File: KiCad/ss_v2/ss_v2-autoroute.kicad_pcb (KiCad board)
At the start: 2 copper layers, 59 parts, among them J1 PJ-313D-B-SMT, J2 UJC-HP-M-G-5-MSMT-TR, J3 DC-005-20A, J4 Conn_02x03_Top_Bottom, J5 Conn_02x03_Counter_Clockwise, J6 Conn_01x08_Pin, J7 Conn_01x04, Q1 BSN20, Q2 IRF7416TRPBF, Q3 BSN20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

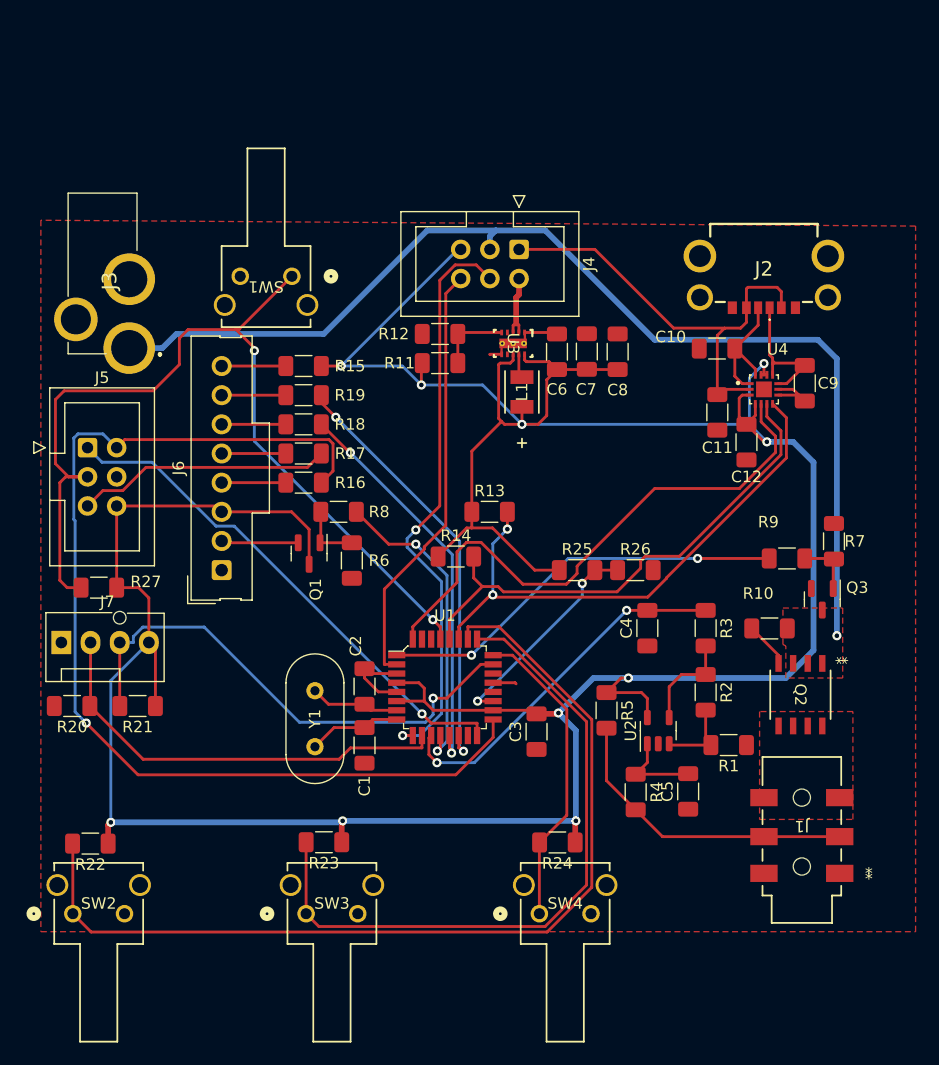
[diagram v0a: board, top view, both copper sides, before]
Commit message: Autorouting verbessert
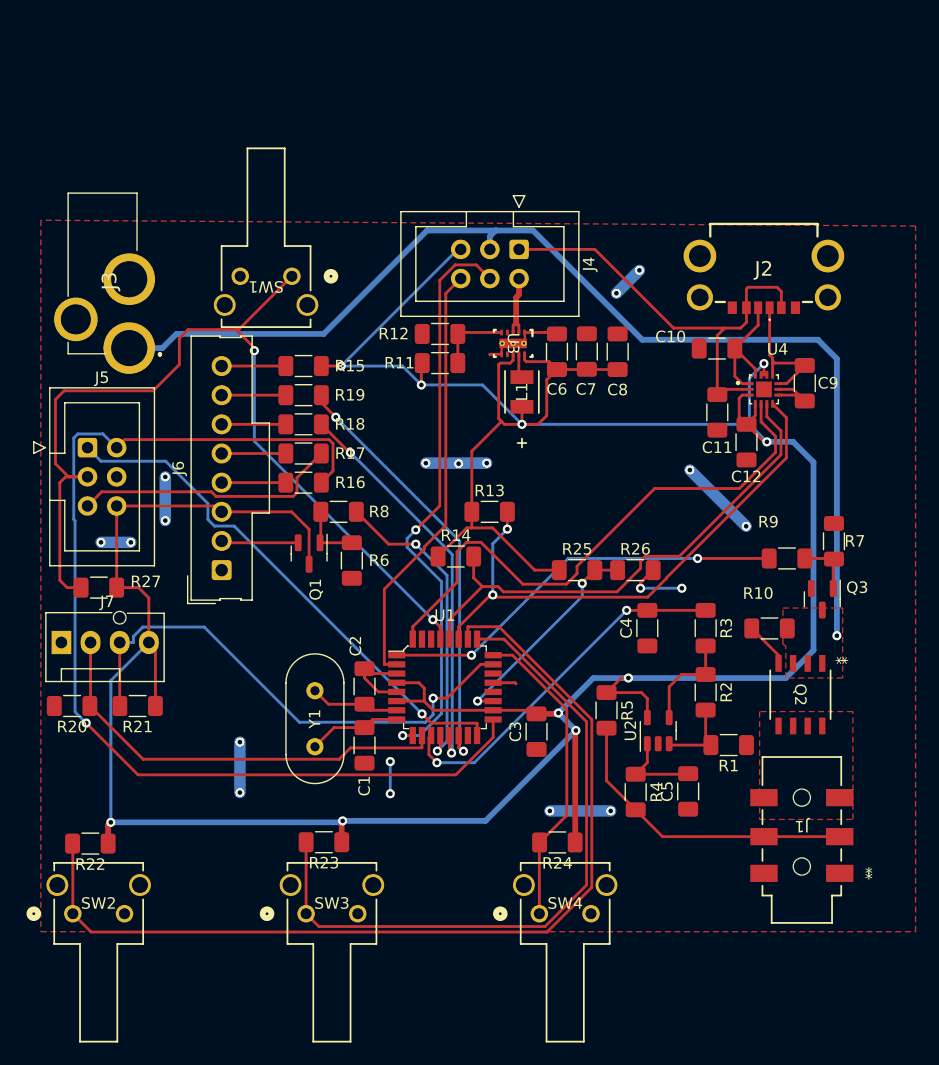
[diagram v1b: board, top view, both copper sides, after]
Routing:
- net GND: track 18.3 -> 57.9 mm, vias 0 -> 19
- net +5V: track 310.1 -> 313.3 mm
- net mosi: track 22.3 -> 23.3 mm
- net miso: track 45.0 -> 45.8 mm

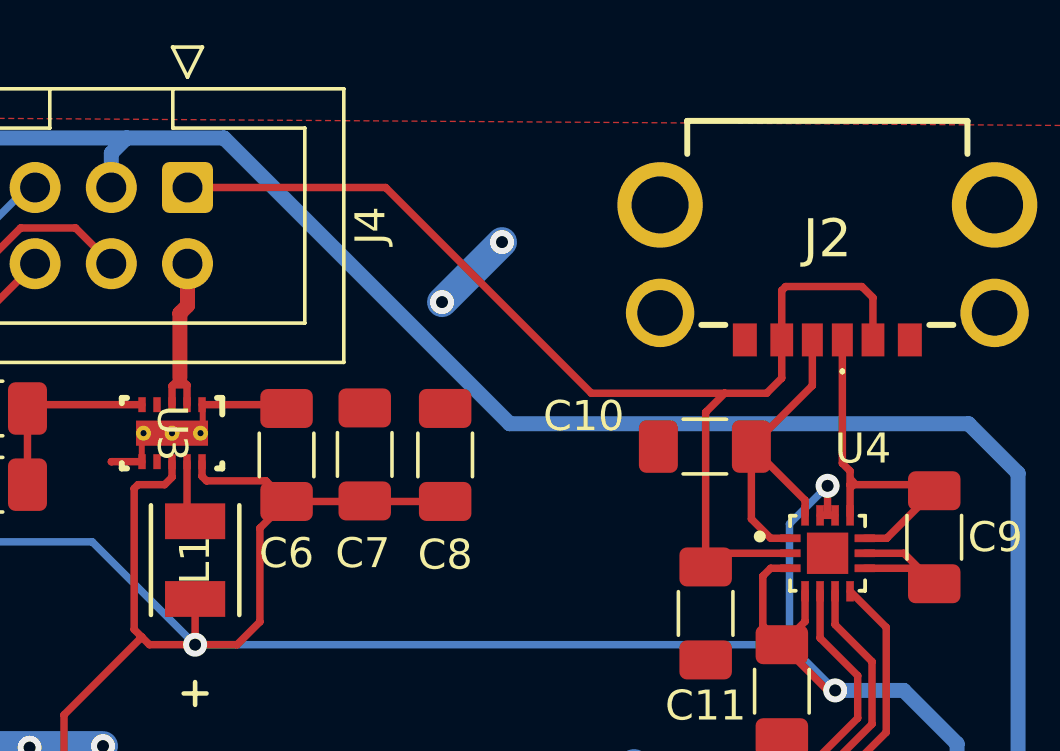
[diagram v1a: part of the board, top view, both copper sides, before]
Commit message: Autorouting verbessert
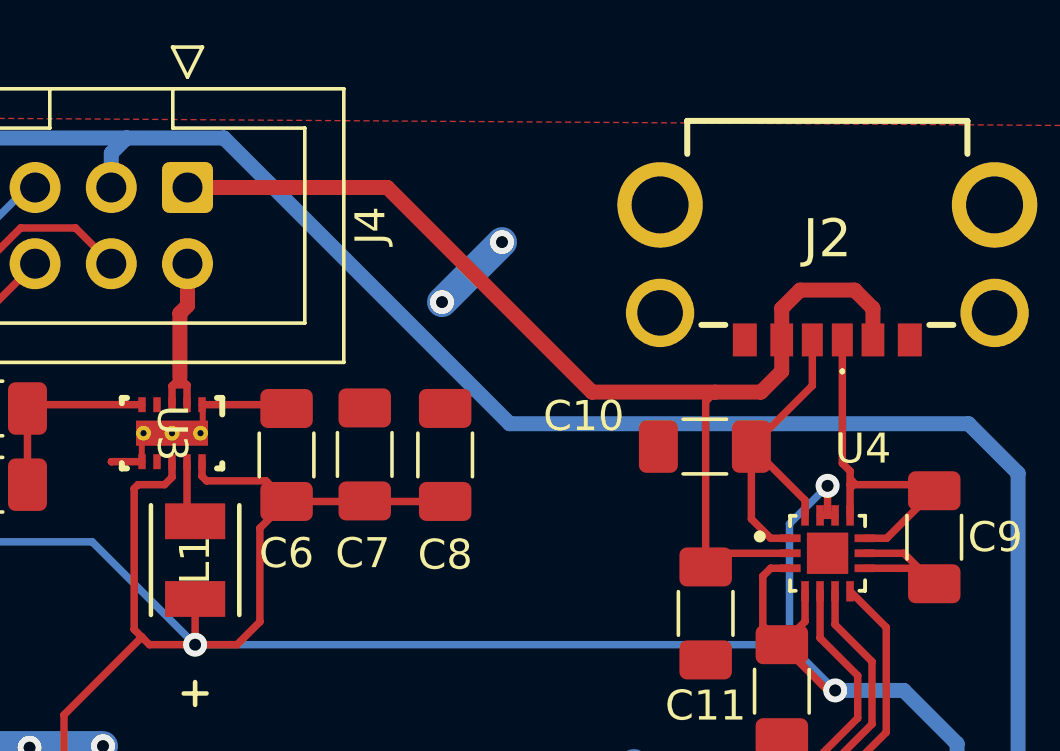
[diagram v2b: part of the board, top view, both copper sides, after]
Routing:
- net VBUS: track 39.5 -> 38.6 mm
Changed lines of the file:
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@@
   (segment (start 249.055 80.272) (end 248.412 79.629) (width 0.25) (layer "F.Cu") (net 8))
   (segment (start 250.202 79.006) (end 248.412 77.216) (width 0.25) (layer "F.Cu") (net 8))
-  (segment (start 243.078 75.438) (end 247.523 75.438) (width 0.25) (layer "F.Cu") (net 9))
-  (segment (start 246.888 81.228) (end 246.888 76.073) (width 0.25) (layer "F.Cu") (net 9))
+  (segment (start 251.854 72) (end 252.464 72.61) (width 0.5) (layer "F.Cu") (net 9))
+  (segment (start 252.464 72.61) (end 252.464 73.66) (width 0.5) (layer "F.Cu") (net 9))
   (segment (start 249.712 80.772) (end 247.344 80.772) (width 0.25) (layer "F.Cu") (net 9))
-  (segment (start 249.424 72.013) (end 249.555 71.882) (width 0.25) (layer "F.Cu") (net 9))
-  (segment (start 229.616 68.58) (end 236.22 68.58) (width 0.25) (layer "F.Cu") (net 9))
-  (segment (start 249.424 73.66) (end 249.424 72.013) (width 0.25) (layer "F.Cu") (net 9))
-  (segment (start 249.555 71.882) (end 252.095 71.882) (width 0.25) (layer "F.Cu") (net 9))
-  (segment (start 247.523 75.438) (end 248.92 75.438) (width 0.25) (layer "F.Cu") (net 9))
-  (segment (start 236.22 68.58) (end 243.078 75.438) (width 0.25) (layer "F.Cu") (net 9))
-  (segment (start 248.92 75.438) (end 249.424 74.934) (width 0.25) (layer "F.Cu") (net 9))
-  (segment (start 252.095 71.882) (end 252.464 72.251) (width 0.25) (layer "F.Cu") (net 9))
-  (segment (start 246.888 76.073) (end 247.523 75.438) (width 0.25) (layer "F.Cu") (net 9))
+  (segment (start 236.28 68.58) (end 229.616 68.58) (width 0.5) (layer "F.Cu") (net 9))
+  (segment (start 246.888 75.712) (end 247.2 75.4) (width 0.25) (layer "F.Cu") (net 9))
+  (segment (start 249.424 73.66) (end 249.424 72.61) (width 0.5) (layer "F.Cu") (net 9))
+  (segment (start 249.424 73.66) (end 249.424 74.71) (width 0.5) (layer "F.Cu") (net 9))
+  (segment (start 243.1 75.4) (end 236.28 68.58) (width 0.5) (layer "F.Cu") (net 9))
+  (segment (start 250.034 72) (end 251.854 72) (width 0.5) (layer "F.Cu") (net 9))
+  (segment (start 249.424 72.61) (end 250.034 72) (width 0.5) (layer "F.Cu") (net 9))
+  (segment (start 248.734 75.4) (end 247.2 75.4) (width 0.5) (layer "F.Cu") (net 9))
+  (segment (start 247.2 75.4) (end 243.1 75.4) (width 0.5) (layer "F.Cu") (net 9))
+  (segment (start 246.888 81.228) (end 246.888 75.712) (width 0.25) (layer "F.Cu") (net 9))
+  (segment (start 249.424 74.71) (end 248.734 75.4) (width 0.5) (layer "F.Cu") (net 9))
   (segment (start 247.344 80.772) (end 246.888 81.228) (width 0.25) (layer "F.Cu") (net 9))
-  (segment (start 252.464 72.251) (end 252.464 73.66) (width 0.25) (layer "F.Cu") (net 9))
-  (segment (start 249.424 74.934) (end 249.424 73.66) (width 0.25) (layer "F.Cu") (net 9))
   (segment (start 250.9516 119.736) (end 257.5506 119.736) (width 0.25) (layer "F.Cu") (net 10))
   (segment (start 237.236 114.86) (end 239.776 117.4) (width 0.25) (layer "F.Cu") (net 10))

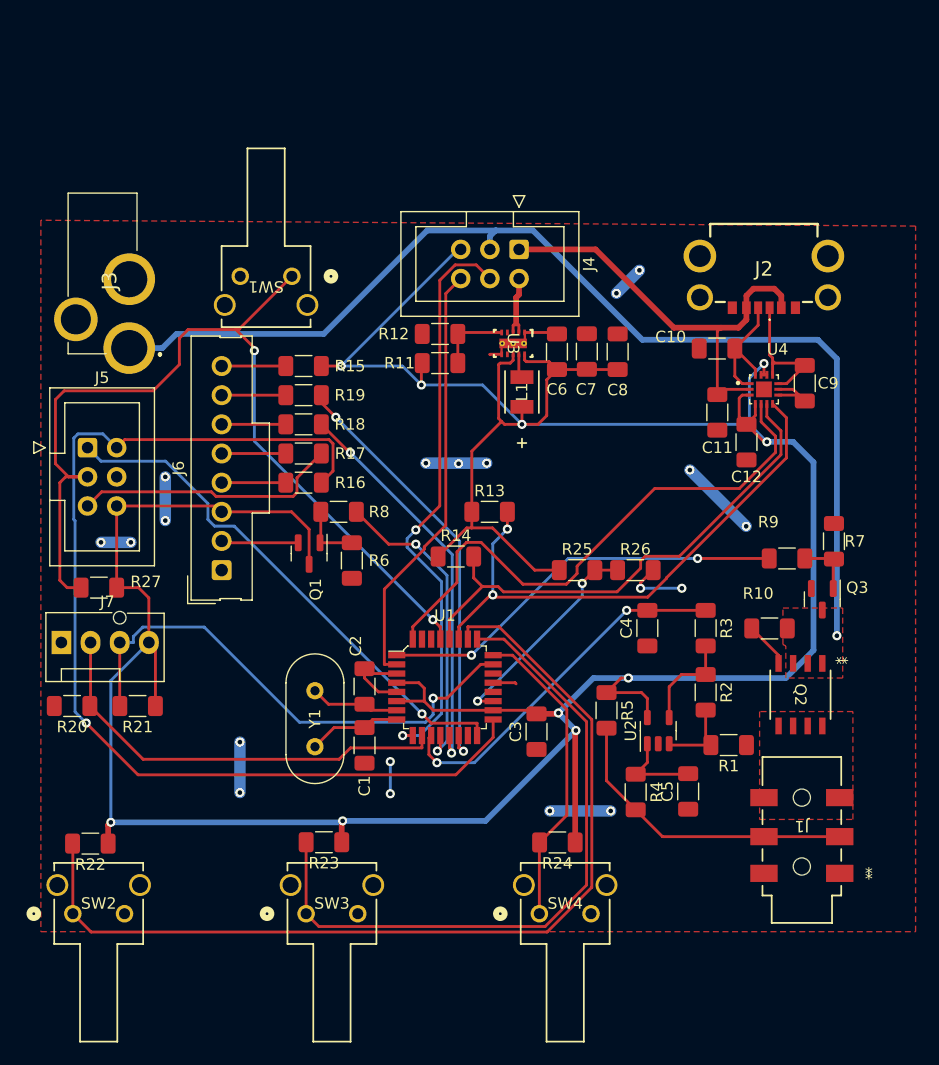
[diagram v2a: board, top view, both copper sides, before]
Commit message: Anpassen des Layouts
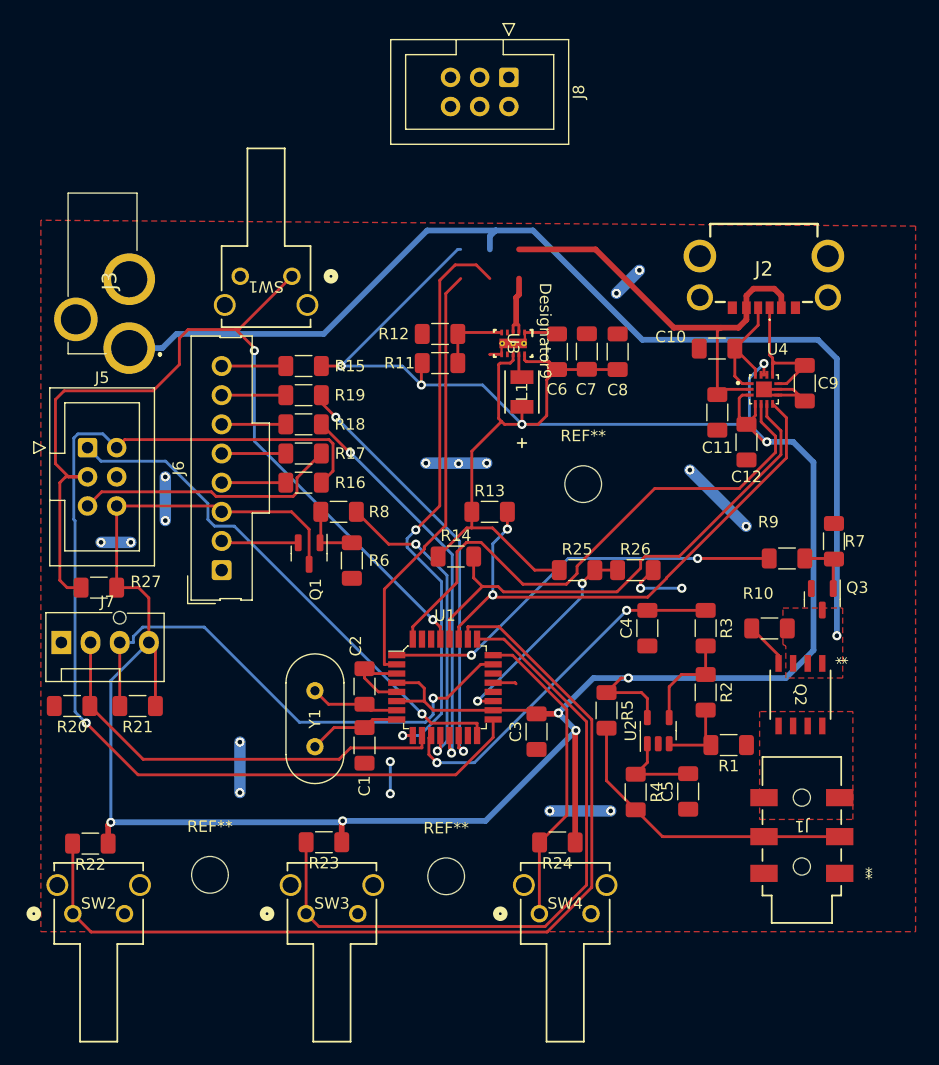
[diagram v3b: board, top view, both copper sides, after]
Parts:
- removed J4: Conn_02x03_Top_Bottom, Connector_IDC:IDC-Header_2x03_P2.54mm_Vertical
- added J8: Conn_02x03_Odd_Even, Connector_IDC:IDC-Header_2x03_P2.54mm_Vertical, F.Cu at (228.7, 53.6)
- added REF**: MountingHole_3.2mm_M3, MountingHole:MountingHole_3.2mm_M3, F.Cu at (202.7, 123.1)
- added REF**: MountingHole_3.2mm_M3, MountingHole:MountingHole_3.2mm_M3, F.Cu at (235.2, 89.0)
- added REF**: MountingHole_3.2mm_M3, MountingHole:MountingHole_3.2mm_M3, F.Cu at (223.3, 123.2)
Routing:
- net GND: track 57.9 -> 60.6 mm

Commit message: Switch-Conn. angepasst.
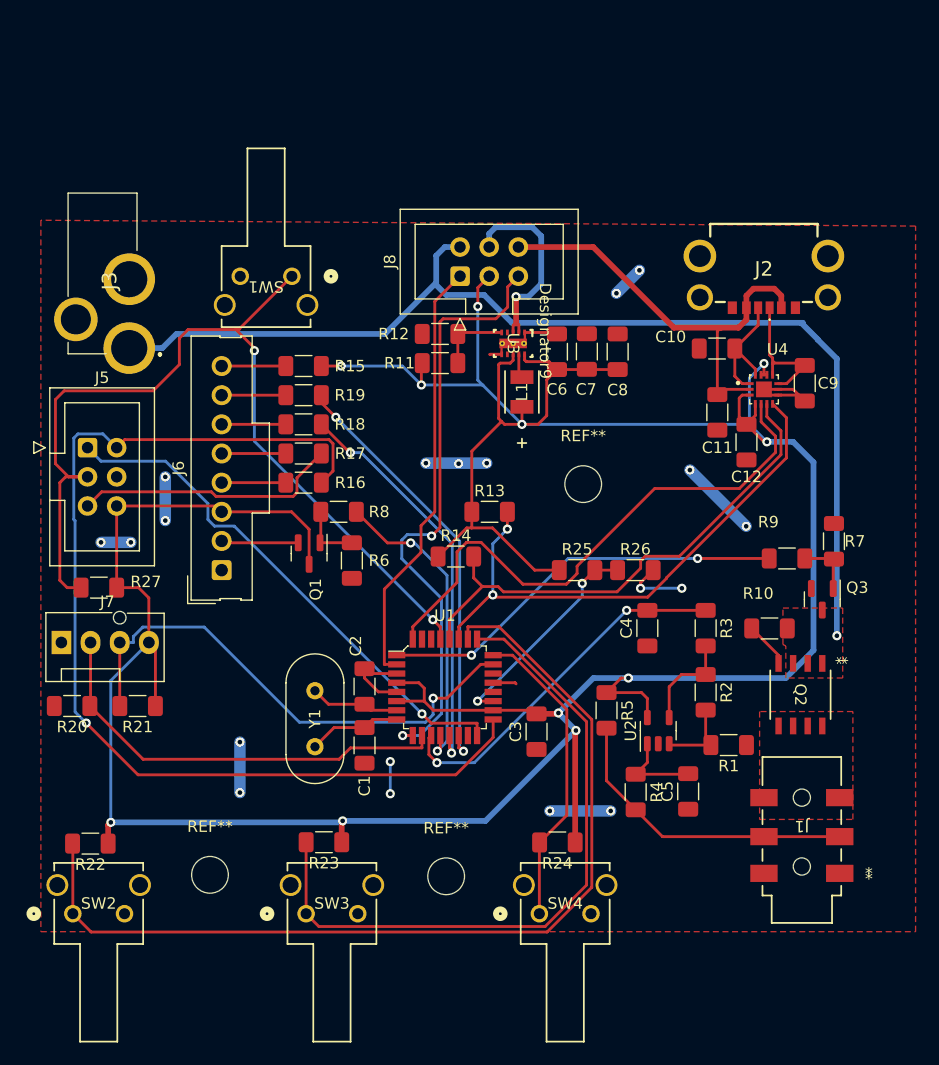
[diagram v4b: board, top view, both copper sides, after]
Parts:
- moved J8 17.8 mm to (224.5, 70.9), turned to 90 degrees
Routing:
- net VDC: track 5.93 -> 17.4 mm, vias 0 -> 1
- net +5V: track 313.3 -> 308.9 mm, vias 10 -> 11
- net sense_usb: track 50.6 -> 52.9 mm
- net dc: track 35.0 -> 35.6 mm

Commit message: ss_v2 mit neuem Chip umgesetzt. Sieht soweit gut aus, keine Probleme festgestellt. Bitte um Überprüfung.
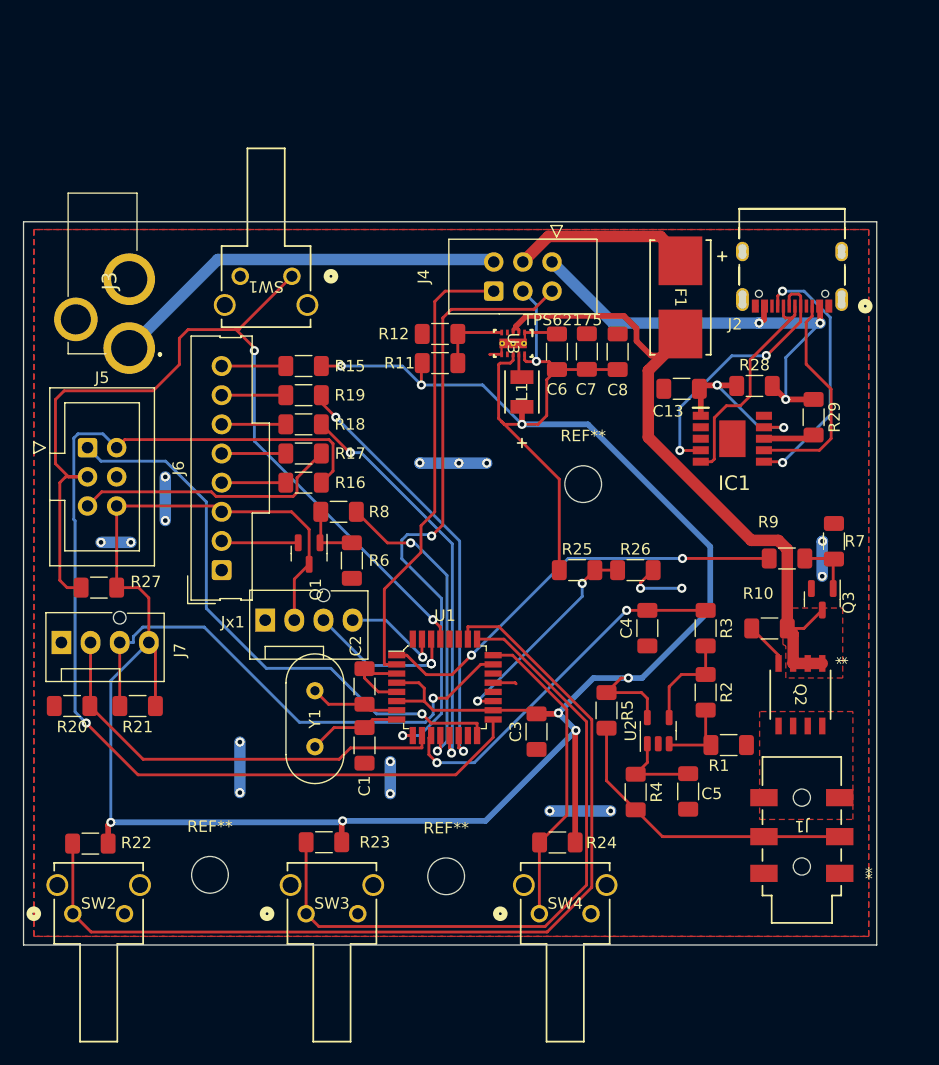
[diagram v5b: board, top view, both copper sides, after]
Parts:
- removed C10, C9: 330p, Resistor_SMD:R_1206_3216Metric_Pad1.30x1.75mm_HandSolder
- removed C11, C12: 100n, Resistor_SMD:R_1206_3216Metric_Pad1.30x1.75mm_HandSolder
- removed J8: Conn_02x03_Odd_Even, Connector_IDC:IDC-Header_2x03_P2.54mm_Vertical
- removed R13, R14: 2k, Resistor_SMD:R_1206_3216Metric_Pad1.30x1.75mm_HandSolder
- removed U4: FUSB302B10MPX, FUSB302B10MPX:QFN50P250X250X80-15N
- added C13: 1u, Resistor_SMD:R_1206_3216Metric_Pad1.30x1.75mm_HandSolder, F.Cu at (243.8, 80.7)
- added F1: 0154003.DR, 0154003:0154Series_LTF, F.Cu at (243.7, 72.8)
- added IC1: CH224K, SOP100P600X180-11N:SOP100P600X180-11N, F.Cu at (248.2, 85.1)
- added J4: Conn_02x03_Top_Bottom, Connector_IDC:IDC-Header_2x03_P2.54mm_Vertical, F.Cu at (227.4, 72.2)
- added Jx1: Conn_01x04, Connector:FanPinHeader_1x04_P2.54mm_Vertical, F.Cu at (207.5, 100.9)
- added R28: 1k, Resistor_SMD:R_1206_3216Metric_Pad1.30x1.75mm_HandSolder, F.Cu at (250.1, 80.5)
- added R29: 10k, Resistor_SMD:R_1206_3216Metric_Pad1.30x1.75mm_HandSolder, F.Cu at (255.3, 83.2)
- J1: footprint PJ-313D-B-SMT:PJ-313D-B-SMT_XKB -> PJ-313D-B-SMT_XKB:PJ-313D-B-SMT_XKB
- J2: value UJC-HP-M-G-5-MSMT-TR -> GT-USB-7004; footprint UJC-HP-M-G-5-MSMT-TR:UJCHPMG5MSMTTR -> CONN12_B-7004_GSW:CONN12_B-7004_GSW
- J3: footprint DC-005-20A:DC00520A -> DC00520A:DC00520A
- L1: footprint NLCV32T-100K-EF:IND_NLCV32T_TDK -> IND_NLCV32T_TDK:IND_NLCV32T_TDK
- Q2: footprint ul_IRF7416TRPBF:SO-8_IRF741_INF -> SO-8_IRF741_INF:SO-8_IRF741_INF
- SW1, SW2, SW3, SW4: footprint ul_TS-1093C-A15:SW_TS-1093C-A15_YDI -> SW_TS-1093C-A15_YDI:SW_TS-1093C-A15_YDI
- U3: footprint TPS62175DQCR:DQC0010A -> DQC0010A:DQC0010A
- moved J2 6.42 mm to (256.1, 73.5)
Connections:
- Q2 pad 1: +12V -> VDC
- Q2 pad 2: +12V -> VDC
- Q2 pad 3: +12V -> VDC
- Q3 pad 3: +12V -> VDC
- R10 pad 2: +12V -> VDC
- U1 pad 27: sda -> unconnected-(U1-PC4-Pad27)
- U1 pad 28: scl -> unconnected-(U1-PC5-Pad28)
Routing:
- net +12V: track 96.2 -> 35.0 mm, vias 1 -> 0
- net sda: track 48.9 -> 0.00 mm, vias 2 -> 0
- net int_n: track 48.7 -> 0.00 mm
- net +5V: track 308.9 -> 262.6 mm, vias 11 -> 9
- net scl: track 45.2 -> 0.00 mm
- net VDC: track 17.4 -> 62.1 mm, vias 1 -> 0
- net dp: track 0.00 -> 23.4 mm, vias 0 -> 2
- net dm: track 0.00 -> 19.9 mm
- net Net-(J4-Pin_2): track 0.00 -> 15.7 mm
- net Net-(IC1-CFG3): track 0.00 -> 14.9 mm, vias 0 -> 2
- net GND: track 60.6 -> 47.1 mm, vias 19 -> 17
- net unconnected-(U1-PD0-Pad30): track 0.00 -> 13.3 mm, vias 0 -> 2
- net cc1: track 11.8 -> 22.6 mm, vias 0 -> 2
- net unconnected-(U1-PD1-Pad31): track 0.00 -> 9.04 mm, vias 0 -> 1
- net cc2: track 11.4 -> 18.9 mm
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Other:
- board outline added: 74.3 x 63 mm
